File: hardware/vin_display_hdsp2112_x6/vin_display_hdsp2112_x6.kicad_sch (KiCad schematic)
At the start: 53 parts, among them J1 DEBUG, J2 USB_B_Micro, J3 DEBUG_UART, J4 IF_UART, J5 AUX_CONNECTOR, Q1 BSS138, SW1 SW_RESET, SW2 BOOTSEL, SW3 KNOB, U1 W25Q16JVSNIQ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

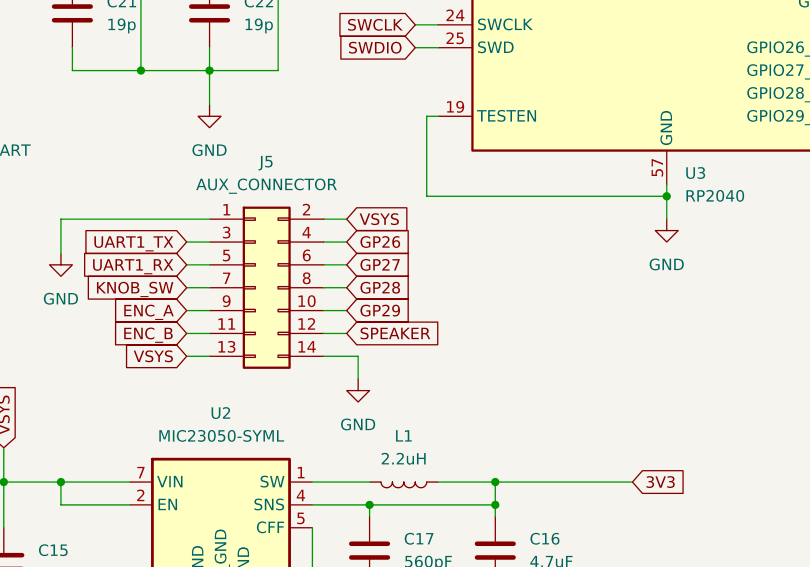
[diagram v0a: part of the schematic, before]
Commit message: work on hdsp2112_x6 pcb
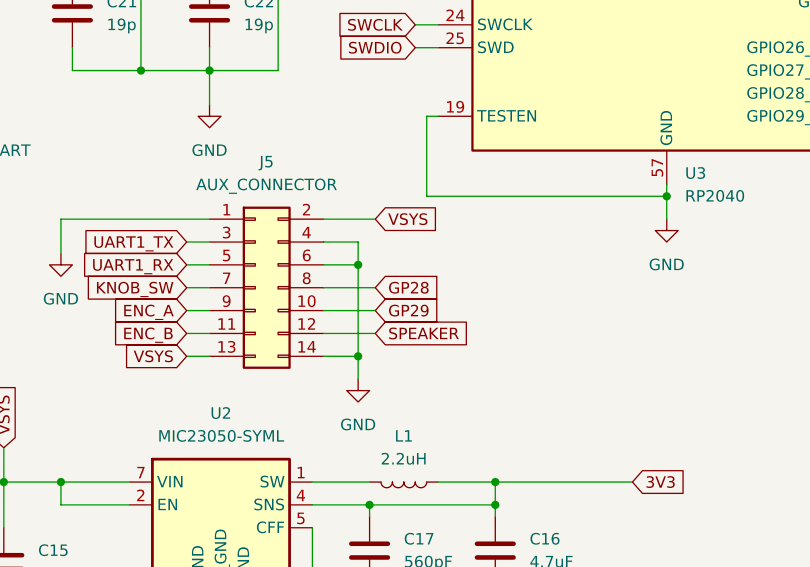
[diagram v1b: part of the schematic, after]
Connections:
- net GP26 is gone; now on net GND: J5.4 (Pin_4)
- net GP27 is gone; now on net GND: J5.6 (Pin_6)
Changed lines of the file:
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@@
   (junction (at 214.63 35.56) (diameter 0) (color 0 0 0 0)
   )
+  (junction (at 119.38 142.24) (diameter 0) (color 0 0 0 0)
+  )
   (junction (at 240.03 132.08) (diameter 0) (color 0 0 0 0)
   )
@@
   )
   (junction (at 102.87 92.71) (diameter 0) (color 0 0 0 0)
+  )
+  (junction (at 119.38 152.4) (diameter 0) (color 0 0 0 0)
   )
   (junction (at 191.77 22.86) (diameter 0) (color 0 0 0 0)
@@
     (stroke (width 0) (type default))
   )
+  (wire (pts (xy 119.38 152.4) (xy 119.38 142.24))
+    (stroke (width 0) (type default))
+  )
   (wire (pts (xy 219.71 87.63) (xy 222.885 87.63))
     (stroke (width 0) (type default))
@@
     (stroke (width 0) (type default))
   )
-  (wire (pts (xy 115.57 149.86) (xy 118.11 149.86))
+  (wire (pts (xy 115.57 149.86) (xy 121.285 149.86))
     (stroke (width 0) (type default))
   )
@@
     (stroke (width 0) (type default))
   )
-  (wire (pts (xy 115.57 147.32) (xy 118.11 147.32))
+  (wire (pts (xy 115.57 147.32) (xy 121.285 147.32))
     (stroke (width 0) (type default))
   )
@@
     (stroke (width 0) (type default))
   )
-  (wire (pts (xy 115.57 144.78) (xy 118.11 144.78))
+  (wire (pts (xy 115.57 144.78) (xy 121.285 144.78))
     (stroke (width 0) (type default))
   )
@@
     (stroke (width 0) (type default))
   )
+  (wire (pts (xy 119.38 142.24) (xy 119.38 139.7))
+    (stroke (width 0) (type default))
+  )
   (wire (pts (xy 77.47 107.95) (xy 77.47 110.49))
     (stroke (width 0) (type default))
@@
     (stroke (width 0) (type default))
   )
-  (wire (pts (xy 115.57 137.16) (xy 118.11 137.16))
+  (wire (pts (xy 115.57 137.16) (xy 121.285 137.16))
     (stroke (width 0) (type default))
   )
@@
     (stroke (width 0) (type default))
   )
-  (wire (pts (xy 115.57 139.7) (xy 118.11 139.7))
+  (wire (pts (xy 115.57 139.7) (xy 119.38 139.7))
     (stroke (width 0) (type default))
   )
@@
     (stroke (width 0) (type default))
   )
-  (wire (pts (xy 115.57 142.24) (xy 118.11 142.24))
+  (wire (pts (xy 115.57 142.24) (xy 119.38 142.24))
     (stroke (width 0) (type default))
   )
@@
     (effects (font (size 0.7 0.7) italic) (justify left bottom))
   )
-  (global_label "GP28" (shape input) (at 118.11 144.78 0) (fields_autoplaced)
-    (effects (font (size 1.27 1.27)) (justify left))
-    (property "Intersheetrefs" "${INTERSHEET_REFS}" (at 125.4821 144.7006 0)
+  (global_label "GP28" (shape input) (at 121.285 144.78 0) (fields_autoplaced)
+    (effects (font (size 1.27 1.27)) (justify left))
+    (property "Intersheetrefs" "${INTERSHEET_REFS}" (at 128.6571 144.7006 0)
       (effects (font (size 1.27 1.27)) (justify left) hide)
     )
@@
     )
   )
-  (global_label "GP29" (shape input) (at 118.11 147.32 0) (fields_autoplaced)
-    (effects (font (size 1.27 1.27)) (justify left))
-    (property "Intersheetrefs" "${INTERSHEET_REFS}" (at 125.4821 147.2406 0)
+  (global_label "GP29" (shape input) (at 121.285 147.32 0) (fields_autoplaced)
+    (effects (font (size 1.27 1.27)) (justify left))
+    (property "Intersheetrefs" "${INTERSHEET_REFS}" (at 128.6571 147.2406 0)
       (effects (font (size 1.27 1.27)) (justify left) hide)
     )
@@
     )
   )
-  (global_label "GP27" (shape input) (at 118.11 142.24 0) (fields_autoplaced)
-    (effects (font (size 1.27 1.27)) (justify left))
-    (property "Intersheetrefs" "${INTERSHEET_REFS}" (at 125.4821 142.1606 0)
-      (effects (font (size 1.27 1.27)) (justify left) hide)
-    )
-  )
   (global_label "DISP5_CE" (shape input) (at 270.51 62.23 0) (fields_autoplaced)
     (effects (font (size 1.27 1.27)) (justify left))
@@
     )
   )
-  (global_label "VSYS" (shape input) (at 118.11 137.16 0) (fields_autoplaced)
-    (effects (font (size 1.27 1.27)) (justify left))
-    (property "Intersheetrefs" "${INTERSHEET_REFS}" (at 125.1193 137.0806 0)
+  (global_label "VSYS" (shape input) (at 121.285 137.16 0) (fields_autoplaced)
+    (effects (font (size 1.27 1.27)) (justify left))
+    (property "Intersheetrefs" "${INTERSHEET_REFS}" (at 128.2943 137.0806 0)
       (effects (font (size 1.27 1.27)) (justify left) hide)
     )
@@
     )
   )
-  (global_label "SPEAKER" (shape input) (at 118.11 149.86 0) (fields_autoplaced)
-    (effects (font (size 1.27 1.27)) (justify left))
-    (property "Intersheetrefs" "${INTERSHEET_REFS}" (at 128.9293 149.7806 0)
+  (global_label "SPEAKER" (shape input) (at 121.285 149.86 0) (fields_autoplaced)
+    (effects (font (size 1.27 1.27)) (justify left))
+    (property "Intersheetrefs" "${INTERSHEET_REFS}" (at 132.1043 149.7806 0)
       (effects (font (size 1.27 1.27)) (justify left) hide)
     )
@@
     )
   )
-  (global_label "GP26" (shape input) (at 118.11 139.7 0) (fields_autoplaced)
-    (effects (font (size 1.27 1.27)) (justify left))
-    (property "Intersheetrefs" "${INTERSHEET_REFS}" (at 125.4821 139.6206 0)
-      (effects (font (size 1.27 1.27)) (justify left) hide)
-    )
-  )
